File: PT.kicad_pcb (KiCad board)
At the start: 4 copper layers, 67 x 68 mm, 110 parts, among them J1 Conn_02x05_Odd_Even, J10 Screw_Terminal_01x05, J11 RJ45_Hanrun_HR911105A_Horizon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, J2 Conn_02x01, J3 Conn_02x01, J4 Conn_02x01, J5 Conn_02x01, J6 Screw_Terminal_01x02, J7 USB_C_Receptacle_USB2.0_16P, J8 Conn_02x01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

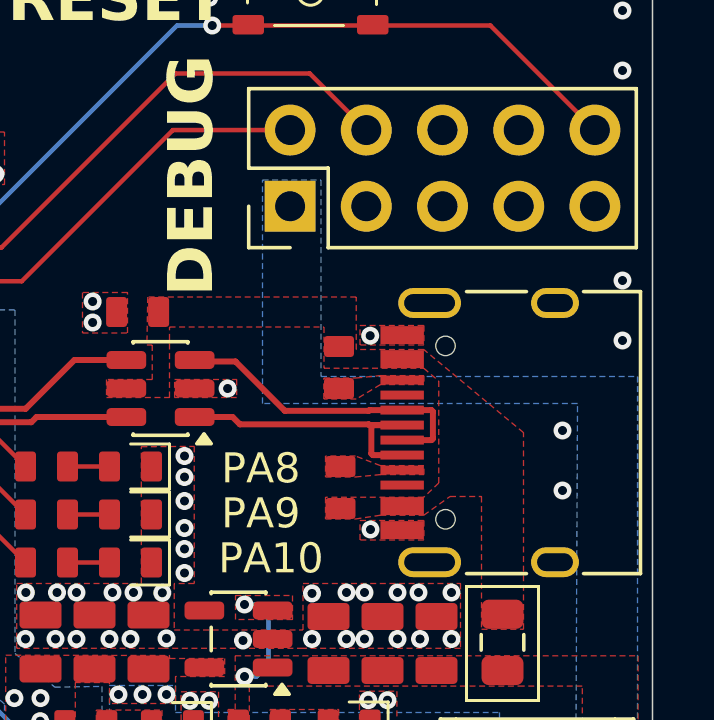
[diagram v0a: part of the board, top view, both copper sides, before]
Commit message: Device is a sink not a source
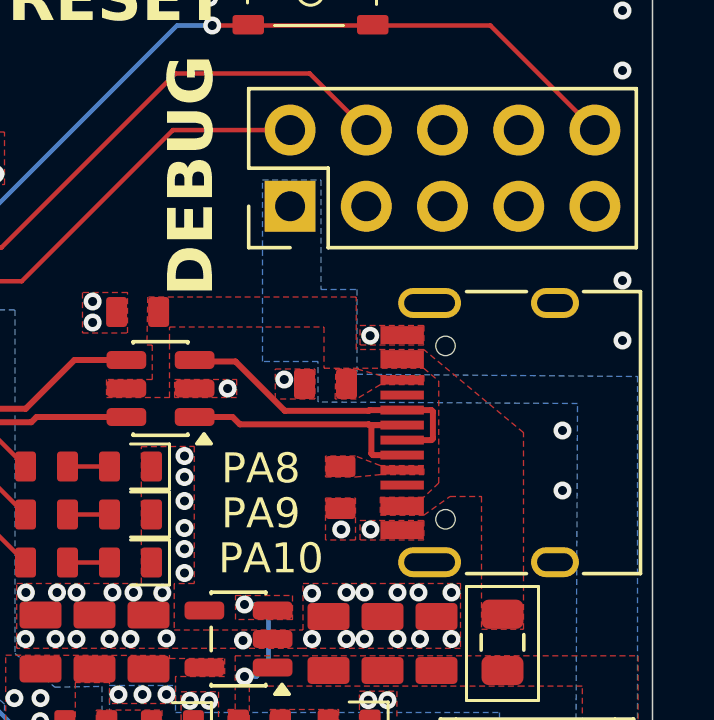
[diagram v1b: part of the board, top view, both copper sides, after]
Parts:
- moved R16 0.71 mm to (153.7, 106.8), turned to 180 degrees
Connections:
- R15 pad 1: Net-(U8-VBUS) -> GND
- R15 pad 2: Net-(J7-CC1) -> Net-(J7-CC2)
- R16 pad 1: Net-(U8-VBUS) -> Net-(J7-CC1)
- R16 pad 2: Net-(J7-CC2) -> GND
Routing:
- net GND: vias 316 -> 318
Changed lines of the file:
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@@
 			(layers "F.Cu" "F.Mask" "F.Paste")
 			(roundrect_rratio 0.15)
-			(net 17 "Net-(U8-VBUS)")
+			(net 1 "GND")
 			(pintype "passive")
 		)
@@
 			(layers "F.Cu" "F.Mask" "F.Paste")
 			(roundrect_rratio 0.15)
-			(net 56 "Net-(J7-CC1)")
+			(net 58 "Net-(J7-CC2)")
 			(pintype "passive")
 		)
@@
 	(footprint "aprlprints:R_0603-noct"
 		(layer "F.Cu")
-		(at 154.15 106.225 -90)
+		(at 153.7 106.775 180)
 		(property "Reference" "R16"
-			(at 0 -1.4 270)
+			(at 0 -1.4 180)
 			(unlocked yes)
 			(layer "F.SilkS")
@@
 		)
 		(property "Value" "4.7k"
-			(at 0 1 270)
+			(at 0 1 180)
 			(unlocked yes)
 			(layer "F.Fab")
@@
 		)
 		(property "Datasheet" "~"
-			(at 0 0 270)
+			(at 0 0 180)
 			(unlocked yes)
 			(layer "F.Fab")
@@
 		)
 		(property "Description" "Resistor, small US symbol"
-			(at 0 0 270)
+			(at 0 0 180)
 			(unlocked yes)
 			(layer "F.Fab")
@@
 		(attr through_hole)
 		(fp_text user "${REFERENCE}"
-			(at 0 2.5 270)
+			(at 0 2.5 180)
 			(unlocked yes)
 			(layer "F.Fab")
@@
 		)
 		(pad "1" smd roundrect
-			(at -0.7 0 270)
+			(at -0.7 0 180)
 			(size 0.7 1)
 			(layers "F.Cu" "F.Mask" "F.Paste")
 			(roundrect_rratio 0.15)
-			(net 17 "Net-(U8-VBUS)")
+			(net 56 "Net-(J7-CC1)")
 			(pintype "passive")
 		)
 		(pad "2" smd roundrect
-			(at 0.7 0 270)
+			(at 0.7 0 180)
 			(size 0.7 1)
 			(layers "F.Cu" "F.Mask" "F.Paste")
 			(roundrect_rratio 0.15)
-			(net 58 "Net-(J7-CC2)")
+			(net 1 "GND")
 			(pintype "passive")
 		)
@@
 	)
 	(via
+		(at 154.225 111.625)
+		(size 0.6)
+		(drill 0.3)
+		(layers "F.Cu" "B.Cu")
+		(free yes)
+		(net 1)
+	)
+	(via
 		(at 129.925 94.625)
 		(size 0.6)
@@
 	)
 	(via
+		(at 152.325 106.625)
+		(size 0.6)
+		(drill 0.3)
+		(layers "F.Cu" "B.Cu")
+		(free yes)
+		(net 1)
+	)
+	(via
 		(at 130.3 131.875)
 		(size 0.6)
@@
 		(layer "F.Cu")
 		(hatch edge 0.5)
+		(priority 63)
+		(connect_pads yes
+			(clearance 0)
+		)
+		(min_thickness 0.25)
+		(filled_areas_thickness no)
+		(fill yes
+			(thermal_gap 0.5)
+			(thermal_bridge_width 0.5)
+		)
+		(polygon
+			(pts
+				(xy 153.7 110.575) (xy 154.7 110.575) (xy 154.7 111.975) (xy 153.7 111.975)
+			)
+		)
+	)
+	(zone
+		(net 1)
+		(net_name "GND")
+		(layer "F.Cu")
+		(hatch edge 0.5)
 		(priority 48)
 		(connect_pads yes
@@
 		(polygon
 			(pts
-				(xy 156.98 106.795) (xy 155.53 106.795) (xy 154.73 107.275) (xy 153.645 107.275) (xy 153.645 106.575)
-				(xy 154.73 106.575) (xy 155.53 106.495) (xy 156.98 106.495)
+				(xy 156.98 106.795) (xy 155.53 106.795) (xy 154.73 107.275) (xy 154.02 107.275) (xy 154.045 106.275)
+				(xy 154.755 106.275) (xy 155.53 106.495) (xy 156.98 106.495)
 			)
 		)
@@
 			(pts
 				(xy 146.4 107.225) (xy 148.5 107.225) (xy 148.5 104.875) (xy 153.65 104.875) (xy 153.65 106.25)
-				(xy 156.975 106.25) (xy 157.475 106.675) (xy 157.475 110.075) (xy 156.975 110.55) (xy 153.7 110.55)
-				(xy 153.7 111.275) (xy 154.7 111.275) (xy 155.525 111.15) (xy 156.975 111.15) (xy 157.85 110.525)
+				(xy 156.975 106.25) (xy 157.475 106.675) (xy 157.475 110.075) (xy 156.975 110.55) (xy 155.525 110.55)
+				(xy 155.525 111.15) (xy 155.525 111.15) (xy 155.525 111.15) (xy 156.975 111.15) (xy 157.85 110.525)
 				(xy 158.9 110.525) (xy 158.9 114.95) (xy 160.3 114.95) (xy 160.3 108.395) (xy 156.975 105.625) (xy 154.725 105.625)
 				(xy 154.725 103.875) (xy 147.775 103.875) (xy 147.746365 105.474934) (xy 147.925 105.475) (xy 147.925 106.625)
@@
 		(layer "F.Cu")
 		(hatch edge 0.5)
+		(priority 74)
+		(connect_pads yes
+			(clearance 0)
+		)
+		(min_thickness 0.25)
+		(filled_areas_thickness no)
+		(fill yes
+			(thermal_gap 0.5)
+			(thermal_bridge_width 0.5)
+		)
+		(polygon
+			(pts
+				(xy 153.35 106.275) (xy 153.35 107.275) (xy 152.025 107.275) (xy 152.025 106.275)
+			)
+		)
+	)
+	(zone
+		(net 1)
+		(net_name "GND")
+		(layer "F.Cu")
+		(hatch edge 0.5)
 		(priority 20)
 		(connect_pads yes
@@
 		(polygon
 			(pts
-				(xy 153.55 106.525) (xy 164.1 106.525) (xy 164.1 130.875) (xy 161.95 130.875) (xy 157.9 130.875)
-				(xy 157.9 119.075) (xy 146.5 119.075) (xy 146.5 116.825) (xy 148.7 116.825) (xy 148.7 117.725) (xy 159.5 117.725)
-				(xy 159.5 128.625) (xy 161.95 128.625) (xy 162.5 128.625) (xy 162.55 118.275) (xy 162.05 118.275)
-				(xy 162.1 107.425) (xy 151.6 107.425) (xy 151.6 99.975) (xy 153.55 99.975)
+				(xy 153.55 103.625) (xy 154.75 103.625) (xy 154.75 106.45) (xy 164.1 106.525) (xy 164.1 130.875)
+				(xy 161.95 130.875) (xy 157.9 130.875) (xy 157.9 119.075) (xy 146.5 119.075) (xy 146.5 116.825)
+				(xy 148.7 116.825) (xy 148.7 117.725) (xy 159.5 117.725) (xy 159.5 128.625) (xy 161.95 128.625)
+				(xy 162.5 128.625) (xy 162.55 118.275) (xy 162.05 118.275) (xy 162.1 107.425) (xy 153.45 107.375)
+				(xy 153.45 106.025) (xy 151.6 106.025) (xy 151.6 99.975) (xy 153.55 99.975)
 			)
 		)

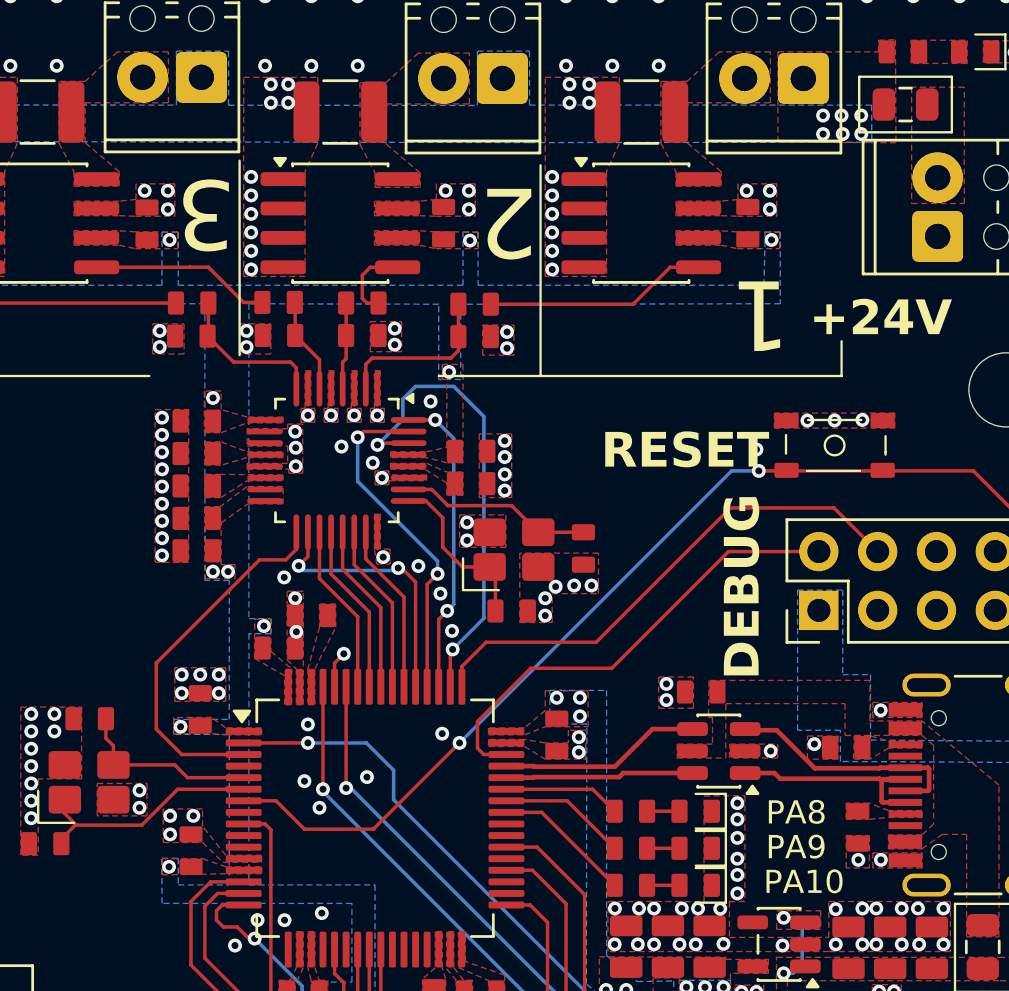
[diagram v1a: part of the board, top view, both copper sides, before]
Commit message: Fix fill problems
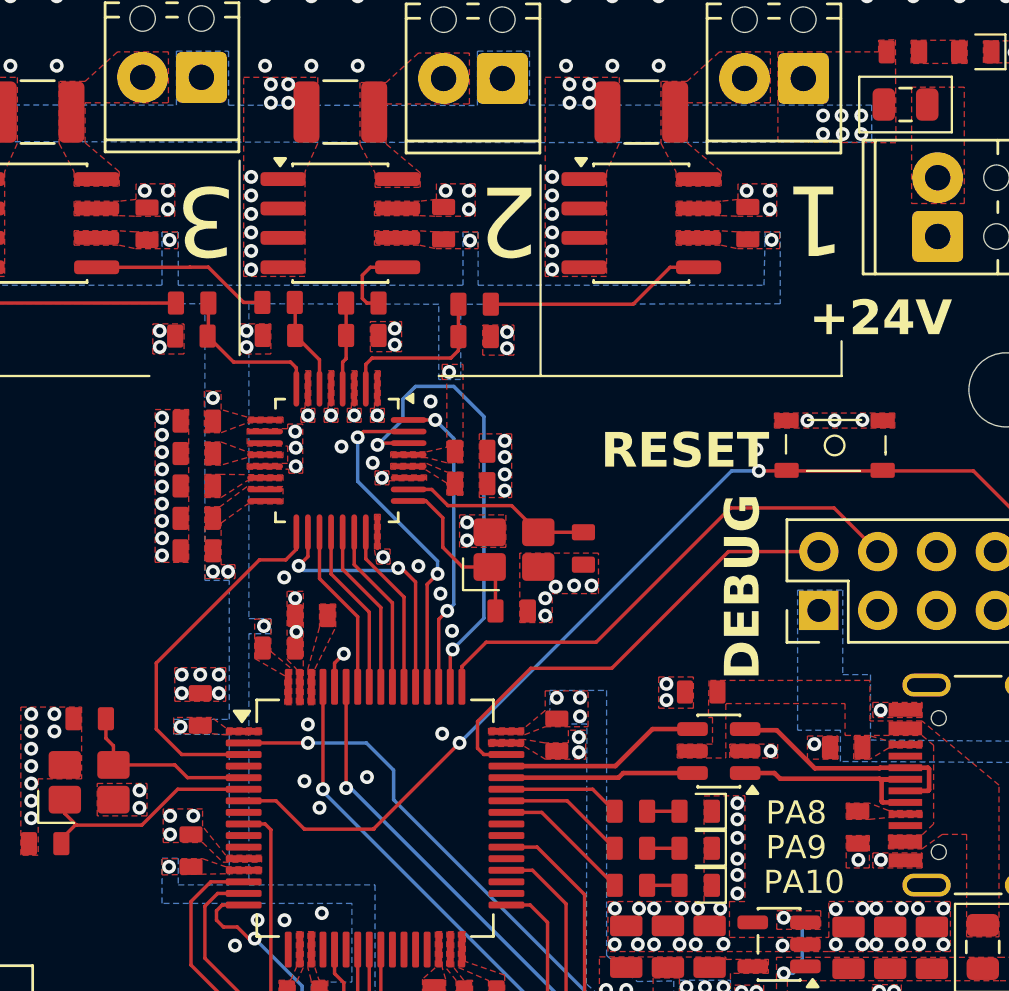
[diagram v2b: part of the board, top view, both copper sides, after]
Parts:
- moved R15 3.49 mm to (153.7, 106.8), turned to 0 degrees
- moved R16 3.49 mm to (154.2, 110.2), turned to -90 degrees

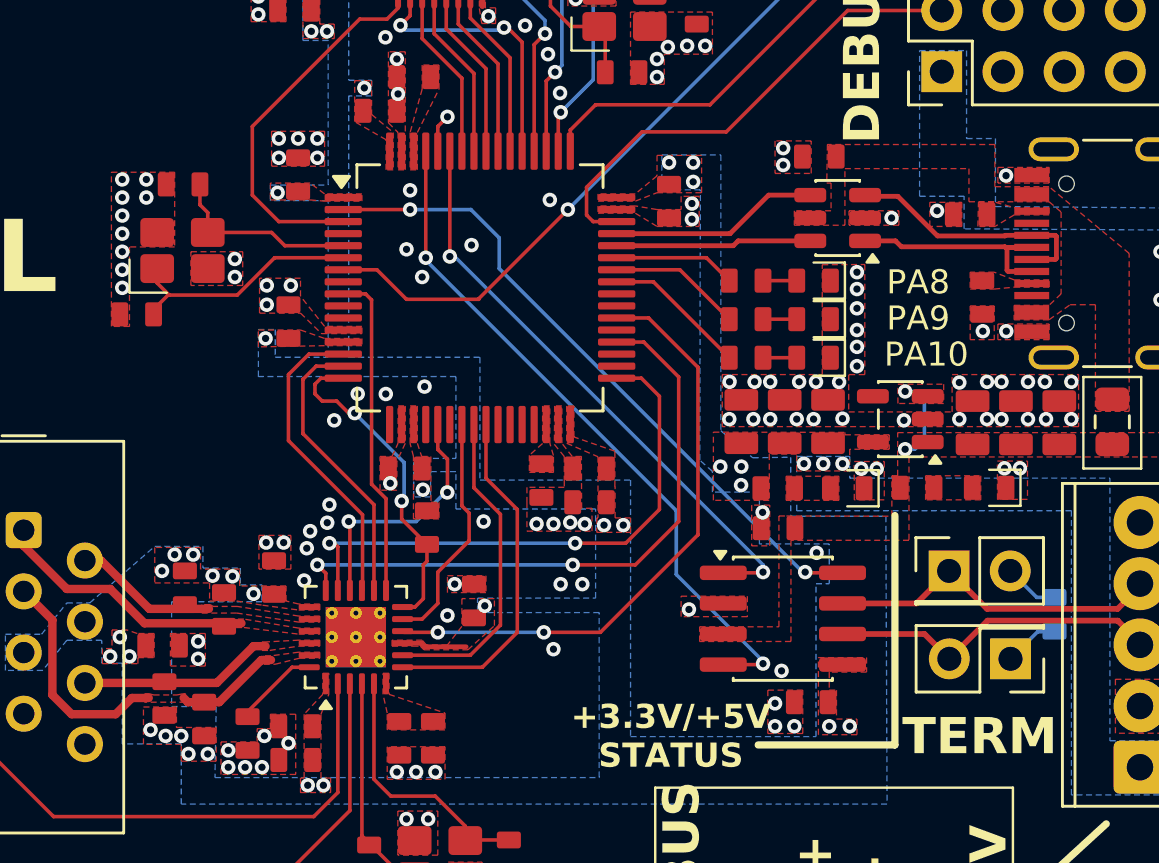
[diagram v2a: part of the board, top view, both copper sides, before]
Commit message: Fix ethernet routing
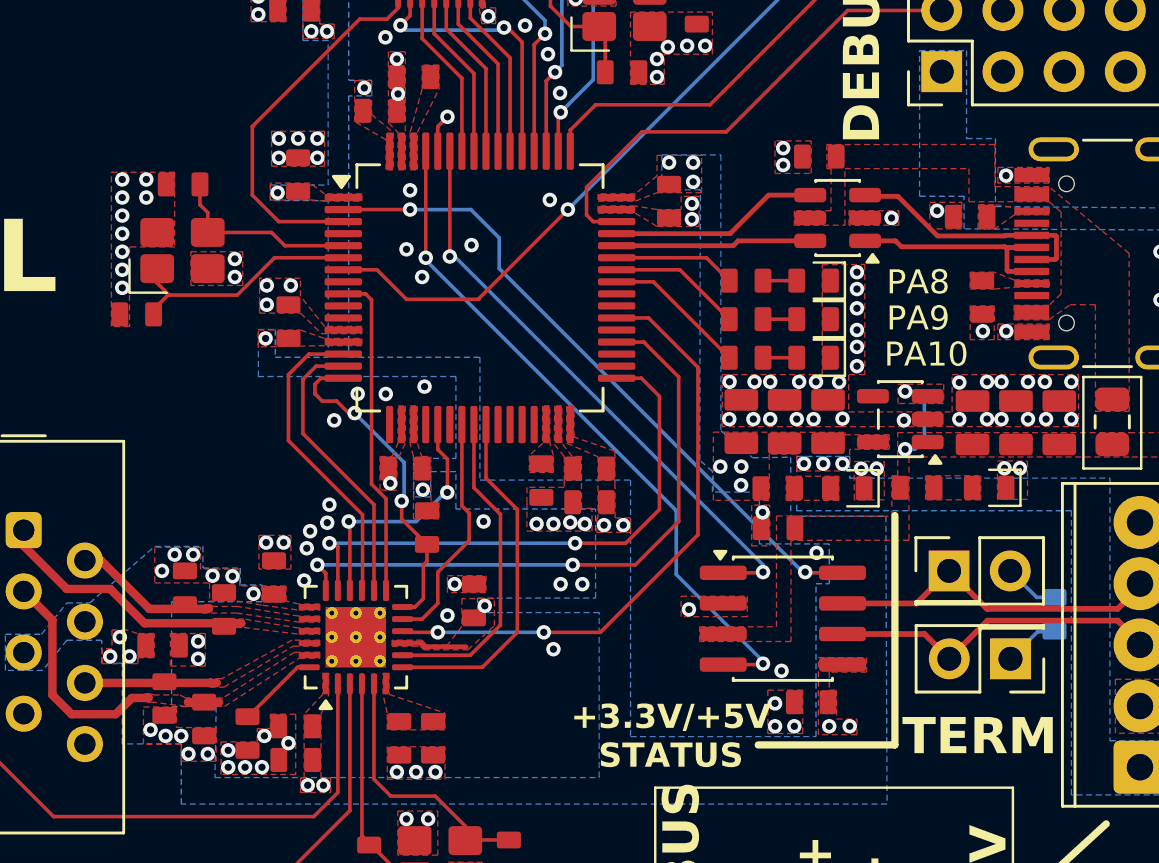
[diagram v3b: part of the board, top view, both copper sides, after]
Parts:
- moved R15 0.10 mm to (153.7, 106.9)
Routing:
- net /Connectivity/RX+: track 13.8 -> 10.7 mm
- net /Connectivity/RX-: track 8.13 -> 5.47 mm
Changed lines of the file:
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@@
 	(footprint "aprlprints:R_0603-noct"
 		(layer "F.Cu")
-		(at 153.7 106.775)
+		(at 153.7 106.875)
 		(property "Reference" "R15"
 			(at 0 -1.4 0)
@@
 	)
 	(segment
-		(start 125.55 125.575)
+		(start 123.7 127.625)
 		(end 123.7 127.425)
 		(width 0.15)
@@
 	(segment
 		(start 126.2625 125.575)
-		(end 125.55 125.575)
+		(end 125.775 125.575)
+		(width 0.15)
+		(layer "F.Cu")
+		(net 50)
+	)
+	(segment
+		(start 123.725 127.625)
+		(end 123.7 127.625)
+		(width 0.15)
+		(layer "F.Cu")
+		(net 50)
+	)
+	(segment
+		(start 125.775 125.575)
+		(end 123.725 127.625)
 		(width 0.15)
 		(layer "F.Cu")
@@
 	)
 	(segment
-		(start 121.225 127.025)
-		(end 121.05 126.85)
-		(width 0.3493)
-		(layer "F.Cu")
-		(net 94)
-	)
-	(segment
 		(start 115.6 123.615)
 		(end 115.6 126.725)
@@
 	)
 	(segment
-		(start 122.525 127.025)
-		(end 124.275 125.275)
-		(width 0.3493)
-		(layer "F.Cu")
-		(net 94)
-	)
-	(segment
 		(start 116.4 127.525)
 		(end 118.225 127.525)
@@
 	)
 	(segment
-		(start 124.275 125.275)
-		(end 124.675 125.275)
-		(width 0.3493)
-		(layer "F.Cu")
-		(net 94)
-	)
-	(segment
-		(start 122.425 126.225)
-		(end 123.95 124.7)
-		(width 0.3493)
-		(layer "F.Cu")
-		(net 95)
-	)
-	(segment
-		(start 123.95 124.7)
-		(end 124.45 124.7)
-		(width 0.3493)
-		(layer "F.Cu")
-		(net 95)
-	)
-	(segment
 		(start 116.95 126.225)
 		(end 122.425 126.225)
@@
 		(polygon
 			(pts
-				(xy 156.98 106.795) (xy 155.53 106.795) (xy 154.73 107.275) (xy 154.02 107.275) (xy 154.045 106.275)
-				(xy 154.755 106.275) (xy 155.53 106.495) (xy 156.98 106.495)
+				(xy 156.98 106.795) (xy 155.53 106.795) (xy 154.73 107.375) (xy 154.02 107.375) (xy 154.045 106.375)
+				(xy 154.755 106.375) (xy 155.53 106.495) (xy 156.98 106.495)
 			)
 		)
@@
 		(polygon
 			(pts
-				(xy 124.3 124.875) (xy 124.625 124.875) (xy 125.825 124.7) (xy 126.7 124.7) (xy 126.7 124.45) (xy 125.825 124.45)
-				(xy 124.45 124.525) (xy 124.3 124.525)
+				(xy 122.125 126.05) (xy 122.125 126.4) (xy 122.725 126.4) (xy 125.6 124.7) (xy 126.7 124.7) (xy 126.7 124.45)
+				(xy 125.55 124.45) (xy 122.625 126.05)
 			)
 		)
@@
 		(polygon
 			(pts
-				(xy 124.375 125.45) (xy 124.85 125.45) (xy 125.85 125.2) (xy 126.7 125.2) (xy 126.7 124.95) (xy 125.825 124.95)
-				(xy 124.675 125.1) (xy 124.375 125.1)
+				(xy 122.4 127.2) (xy 122.75 127.2) (xy 125.85 125.2) (xy 126.7 125.2) (xy 126.7 124.95) (xy 125.65 124.95)
+				(xy 122.675 126.85) (xy 122.4 126.85)
 			)
 		)
@@
 				(xy 155.525 111.15) (xy 156.975 111.15) (xy 157.85 110.525) (xy 158.9 110.525) (xy 158.9 114.95)
 				(xy 160.3 114.95) (xy 160.3 108.395) (xy 156.975 105.625) (xy 154.725 105.625) (xy 154.725 103.875)
-				(xy 147.775 103.875) (xy 147.746365 105.474934) (xy 147.925 105.475) (xy 147.925 106.625) (xy 146.4 106.625)
+				(xy 147.75 103.875) (xy 147.75 104.874934) (xy 147.925 104.875) (xy 147.925 106.625) (xy 146.4 106.625)
 			)
 		)
@@
 		(polygon
 			(pts
-				(xy 119.425 126.675) (xy 119.625 126.675) (xy 119.8 126.725) (xy 120.775 126.725) (xy 121.025 126.675)
-				(xy 121.125 126.675) (xy 121.125 127.025) (xy 119.425 127.025)
+				(xy 119.425 126.675) (xy 119.625 126.675) (xy 119.8 126.725) (xy 120.9 126.725) (xy 121.125 126.85)
+				(xy 121.325 126.85) (xy 121.325 127.2) (xy 121.125 127.2) (xy 119.775 127.025) (xy 119.425 127.025)
 			)
 		)
@@
 				(xy 164.11 128.315) (xy 159.73 128.315) (xy 159.73 126.075) (xy 162.26 126.075) (xy 162.26 116.845)
 				(xy 160.3 116.845) (xy 151.16 116.845) (xy 151.16 120.305) (xy 146.26 120.305) (xy 146.26 124.505)
-				(xy 142.47 124.505) (xy 142.47 123.895) (xy 145.76 123.895) (xy 145.76 119.295) (xy 146.07 119.295)
+				(xy 142.47 124.505) (xy 142.47 123.895) (xy 145.66 123.895) (xy 145.66 119.295) (xy 146.07 119.295)
 				(xy 150.45 119.305) (xy 150.45 117.625) (xy 150.69 117.625) (xy 150.69 115.835) (xy 160.3 115.835)
 				(xy 164.12 115.835)
@@
 		(polygon
 			(pts
-				(xy 153.35 106.275) (xy 153.35 107.275) (xy 152.025 107.275) (xy 152.025 106.275)
+				(xy 153.35 106.275) (xy 153.35 107.375) (xy 152.025 107.375) (xy 152.025 106.275)
 			)
 		)

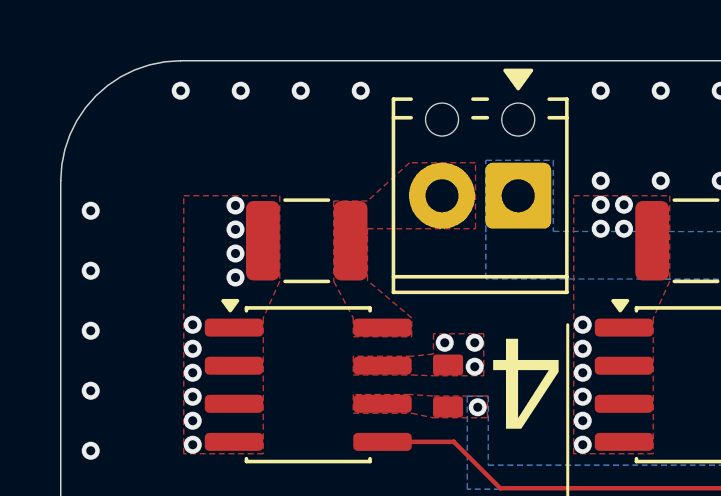
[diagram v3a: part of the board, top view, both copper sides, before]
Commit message: small via spacing
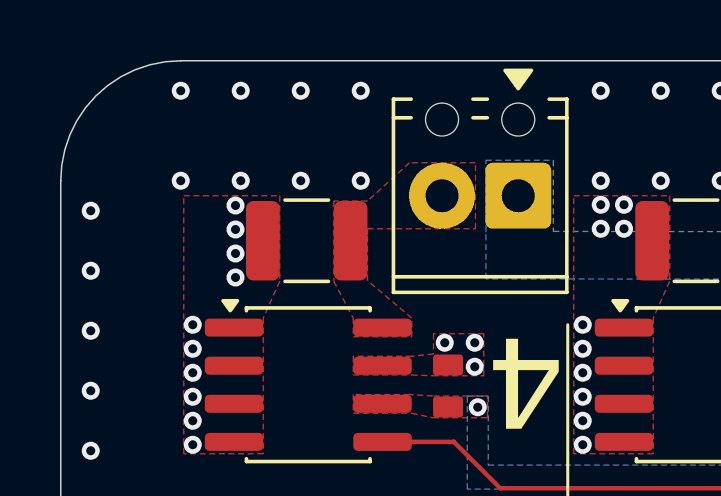
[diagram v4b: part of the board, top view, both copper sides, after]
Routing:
- net GND: vias 318 -> 322
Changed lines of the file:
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@@
 		(layer "Dwgs.User")
 		(pts
-			(xy 101.6 91.325) (xy 97.6 90.325)
+			(xy 101.6 90.325) (xy 97.6 89.325)
 		)
 		(height -19)
@@
 		)
 		(gr_text "4"
-			(at 99.6 71.175 0)
+			(at 99.6 70.175 0)
 			(layer "Dwgs.User")
 			(effects
@@
 	)
 	(via
+		(at 107.6 77.325)
+		(size 0.6)
+		(drill 0.3)
+		(layers "F.Cu" "B.Cu")
+		(free yes)
+		(net 1)
+	)
+	(via
 		(at 160.975 76.75)
 		(size 0.6)
@@
 	)
 	(via
+		(at 103.6 77.325)
+		(size 0.6)
+		(drill 0.3)
+		(layers "F.Cu" "B.Cu")
+		(free yes)
+		(net 1)
+	)
+	(via
 		(at 151.6 140.325)
 		(size 0.6)
@@
 	)
 	(via
+		(at 105.6 77.325)
+		(size 0.6)
+		(drill 0.3)
+		(layers "F.Cu" "B.Cu")
+		(free yes)
+		(net 1)
+	)
+	(via
 		(at 115.6 78.125)
 		(size 0.6)
@@
 		(size 0.6)
 		(drill 0.3)
+		(layers "F.Cu" "B.Cu")
+		(free yes)
+		(net 1)
+	)
+	(via
+		(at 101.6 77.325)
+		(size 0.6)
+		(drill 0.3)
